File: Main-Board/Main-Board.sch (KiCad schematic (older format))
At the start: 24 parts, among them J1 Power_In, J2 ESC_1, J3 ESC_2, J4 ESC_3, J5 ESC_4, J6 Receiver, J7 Aux, U1 MCP6001U

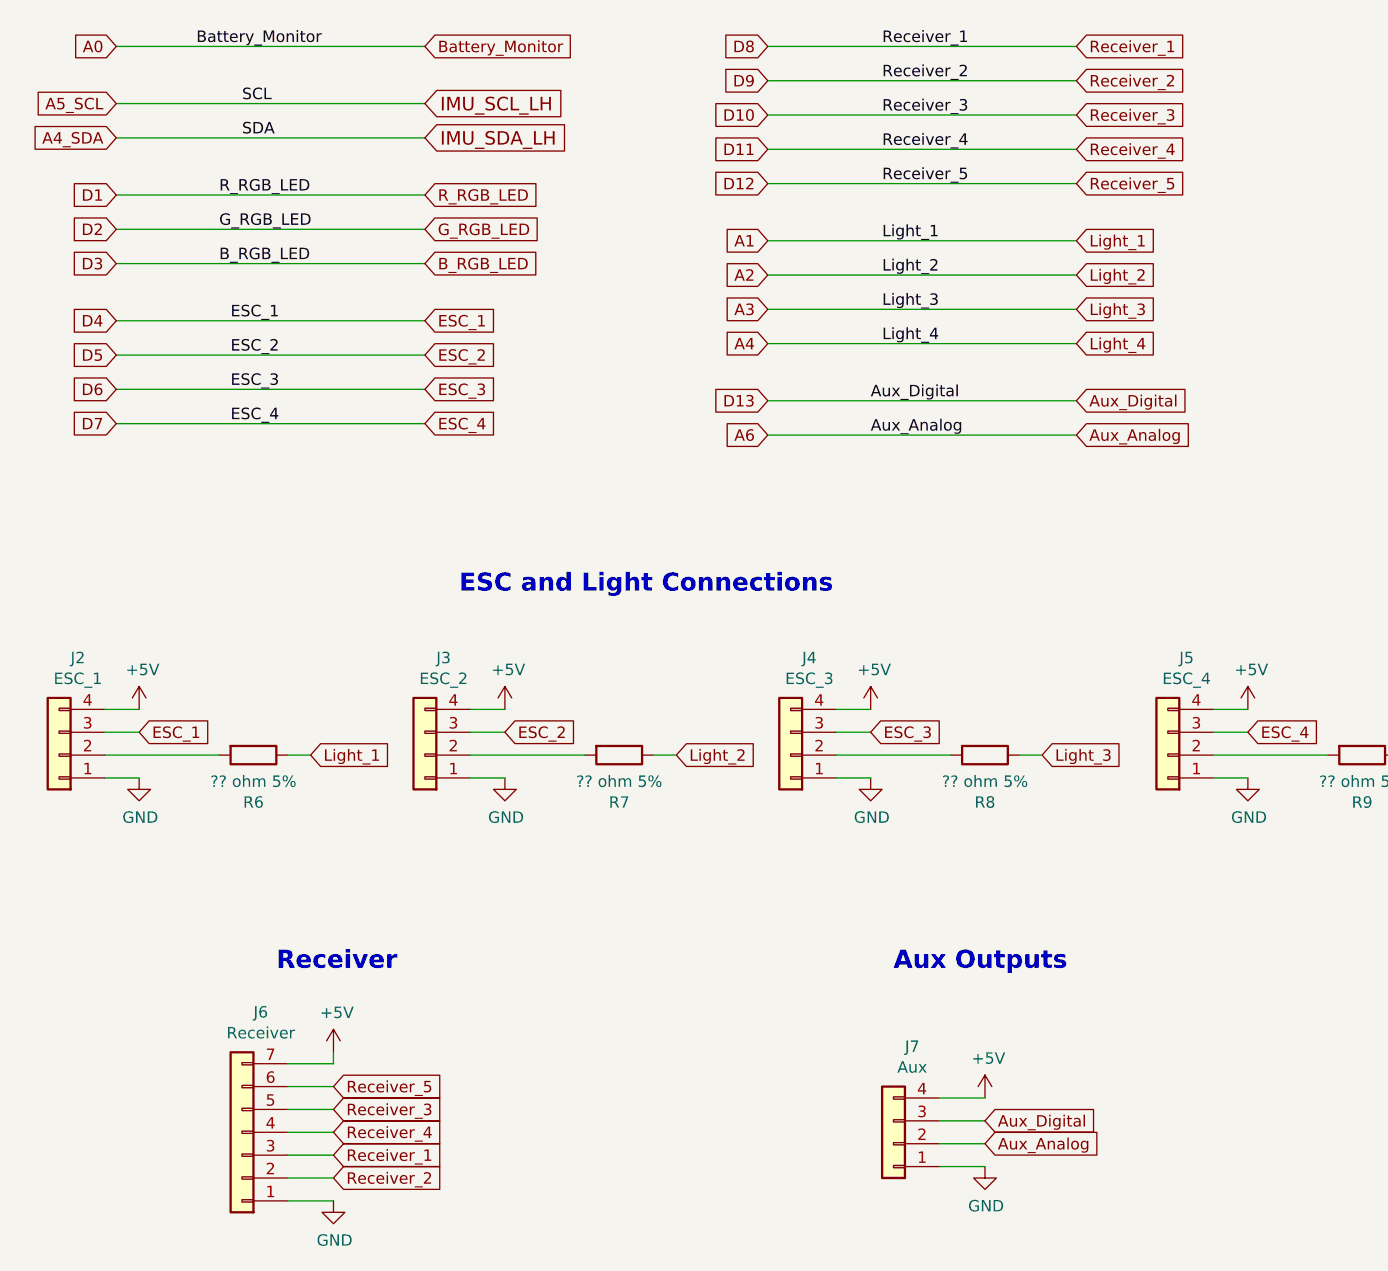
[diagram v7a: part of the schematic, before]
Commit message: add attacheted lights to open ATMEGA ports (A4 cant be used again, dont mess with tx/rx) and removed 5th rc input. Add cap for USB
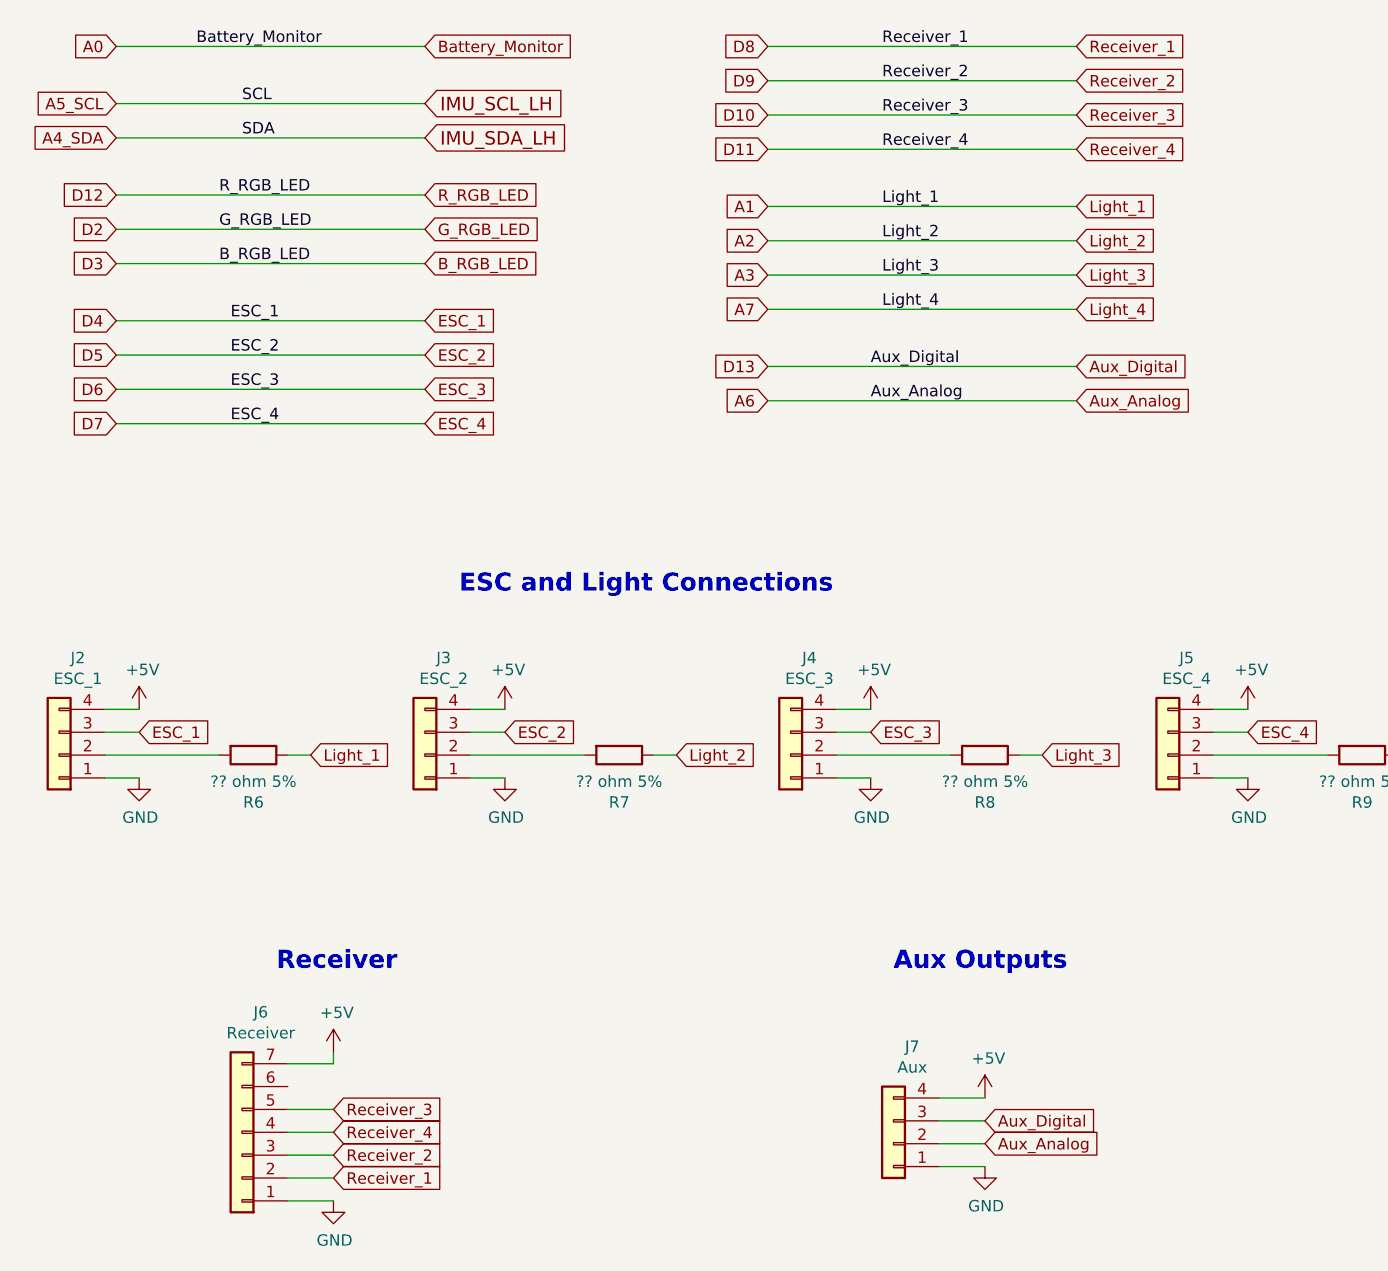
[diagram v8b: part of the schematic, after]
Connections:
- net D1 is gone; now on net D12: R4.1
- net D12: no longer J6.6 (Pin_6)
- net D8: now also J6.2 (Pin_2); no longer J6.3 (Pin_3)
- net D9: now also J6.3 (Pin_3); no longer J6.2 (Pin_2)
- net A4 renamed A7
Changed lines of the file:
@@
 Wire Wire Line
 	5200 2900 3850 2900
-Text GLabel 1000 3100 0    50   Input ~ 0
-D1
 Text GLabel 1000 3250 0    50   Input ~ 0
 D2
@@
 Wire Wire Line
 	1000 2450 2350 2450
+Text GLabel 5200 3150 2    50   Input ~ 0
+Light_1
 Text GLabel 5200 3300 2    50   Input ~ 0
-Light_1
+Light_2
 Text GLabel 5200 3450 2    50   Input ~ 0
-Light_2
+Light_3
 Text GLabel 5200 3600 2    50   Input ~ 0
-Light_3
-Text GLabel 5200 3750 2    50   Input ~ 0
 Light_4
+Text GLabel 3850 3150 0    50   Input ~ 0
+A1
 Text GLabel 3850 3300 0    50   Input ~ 0
-A1
+A2
 Text GLabel 3850 3450 0    50   Input ~ 0
-A2
+A3
 Text GLabel 3850 3600 0    50   Input ~ 0
-A3
-Text GLabel 3850 3750 0    50   Input ~ 0
-A4
-Wire Wire Line
-	3850 3300 5200 3300
-Wire Wire Line
-	5200 3450 3850 3450
-Wire Wire Line
-	3850 3600 5200 3600
-Wire Wire Line
-	5200 3750 3850 3750
+A7
+Wire Wire Line
+	3850 3150 5200 3150
+Wire Wire Line
+	5200 3300 3850 3300
+Wire Wire Line
+	3850 3450 5200 3450
+Wire Wire Line
+	5200 3600 3850 3600
 Text GLabel 1850 5550 2    50   Input ~ 0
 Light_1
@@
 Text Notes 1700 6500 0    79   ~ 16
 Receiver
+Text GLabel 1950 7400 2    50   Input ~ 0
+Receiver_1
 Text GLabel 1950 7300 2    50   Input ~ 0
-Receiver_1
-Text GLabel 1950 7400 2    50   Input ~ 0
 Receiver_2
 Text GLabel 1950 7100 2    50   Input ~ 0
@@
 	1    0    0    -1
 $EndComp
-Text GLabel 3850 3050 0    50   Input ~ 0
+Text GLabel 1000 3100 0    50   Input ~ 0
 D12
-Text GLabel 5200 3050 2    50   Input ~ 0
-Receiver_5
-Wire Wire Line
-	3850 3050 5200 3050
 Text GLabel 1000 3400 0    50   Input ~ 0
 D3
@@
 Text Label 4350 2900 0    50   ~ 0
 Receiver_4
-Text Label 4350 3050 0    50   ~ 0
-Receiver_5
+Text Label 4350 3150 0    50   ~ 0
+Light_1
 Text Label 4350 3300 0    50   ~ 0
-Light_1
+Light_2
 Text Label 4350 3450 0    50   ~ 0
-Light_2
+Light_3
 Text Label 4350 3600 0    50   ~ 0
-Light_3
-Text Label 4350 3750 0    50   ~ 0
 Light_4
-Text GLabel 1950 7000 2    50   Input ~ 0
-Receiver_5
 Wire Wire Line
 	1750 7500 1950 7500
@@
 	1950 6900 1950 6850
 Wire Wire Line
+	1750 7400 1950 7400
+Wire Wire Line
 	1750 7300 1950 7300
 Wire Wire Line
-	1750 7400 1950 7400
-Wire Wire Line
 	1950 7100 1750 7100
 Wire Wire Line
 	1750 7200 1950 7200
-Wire Wire Line
-	1950 7000 1750 7000
 Wire Wire Line
 	7150 2250 7200 2250
@@
 Text Notes 4400 6500 0    79   ~ 16
 Aux Outputs
+Text GLabel 3850 3850 0    50   Input ~ 0
+D13
 Text GLabel 3850 4000 0    50   Input ~ 0
-D13
-Text GLabel 3850 4150 0    50   Input ~ 0
 A6
+Text GLabel 5200 3850 2    50   Input ~ 0
+Aux_Digital
 Text GLabel 5200 4000 2    50   Input ~ 0
+Aux_Analog
+Wire Wire Line
+	3850 3850 5200 3850
+Wire Wire Line
+	5200 4000 3850 4000
+Text Label 4300 3850 0    50   ~ 0
 Aux_Digital
-Text GLabel 5200 4150 2    50   Input ~ 0
-Aux_Analog
-Wire Wire Line
-	3850 4000 5200 4000
-Wire Wire Line
-	5200 4150 3850 4150
 Text Label 4300 4000 0    50   ~ 0
-Aux_Digital
-Text Label 4300 4150 0    50   ~ 0
 Aux_Analog
 Text GLabel 4800 7150 2    50   Input ~ 0
